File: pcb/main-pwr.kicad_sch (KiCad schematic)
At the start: 26 parts, among them U2 ADP5054

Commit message: power restructuring
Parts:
- removed C3, C4, C5, C6, C7: 0.1uF, Capacitor_SMD:C_0402_1005Metric, symbol library:C
- removed L1, L2, L3, L4: 1uH, Inductor_SMD:L_0402_1005Metric, symbol library:L
- removed R10, R8: 24K, Resistor_SMD:R_0402_1005Metric, symbol library:R_US
- removed R11, R14, R7: 30K, Resistor_SMD:R_0402_1005Metric, symbol library:R_US
- removed R12: 120K, Resistor_SMD:R_0402_1005Metric, symbol library:R_US
- removed R13: 15K, Resistor_SMD:R_0402_1005Metric, symbol library:R_US
- removed R15, R17: 100, Resistor_SMD:R_0402_1005Metric, symbol library:R_US
- removed R16: 0.005, Resistor_SMD:R_0603_1608Metric, symbol library:R_US
- removed R6: 31.6K, Resistor_SMD:R_0402_1005Metric, symbol library:R_US
- removed R9: 75K, Resistor_SMD:R_0402_1005Metric, symbol library:R_US
- removed U2: ADP5054, Package_DFN_QFN:QFN-48-1EP_7x7mm_P0.5mm_EP5.15x5.15mm, symbol library:ADP5054
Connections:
- net 5V0_SENS_N: now also C2.1, R3.1; no longer C2.2, R5.1
- net 5V0_SENS_P: now also C2.2, R5.1; no longer C2.1, R3.1
- no-connect marks 2 -> 0
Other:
- removed sheet Comp & Decpl.
- removed sheet Sequencing
- added sheet 1V0 (1v0.kicad_sch)
- added sheet 1V2 (1v2.kicad_sch)
- added sheet 1V35 (1v35.kicad_sch)
- added sheet 1V8 (1v8.kicad_sch)
- added sheet 3V3 (3v3.kicad_sch)
- note added: "Power sequencing: 1. 1V0_FD, 1V0_MGT 2. 1V8_FD 3. 1V2_MGT 4. 1V35_DDR, 3V3_FD"
- note removed: "Power sequencing: 1. 1V0_FD, 1V0_MGT 2. 1V8_FD 3. 1V2_MGT 4. 3V3_FD"
- note removed: "V_en = 0.811V"
- note removed: "vout = vref * (1 + rtop/rbot)"
- moved on the sheet: C2, R3, R4, R5

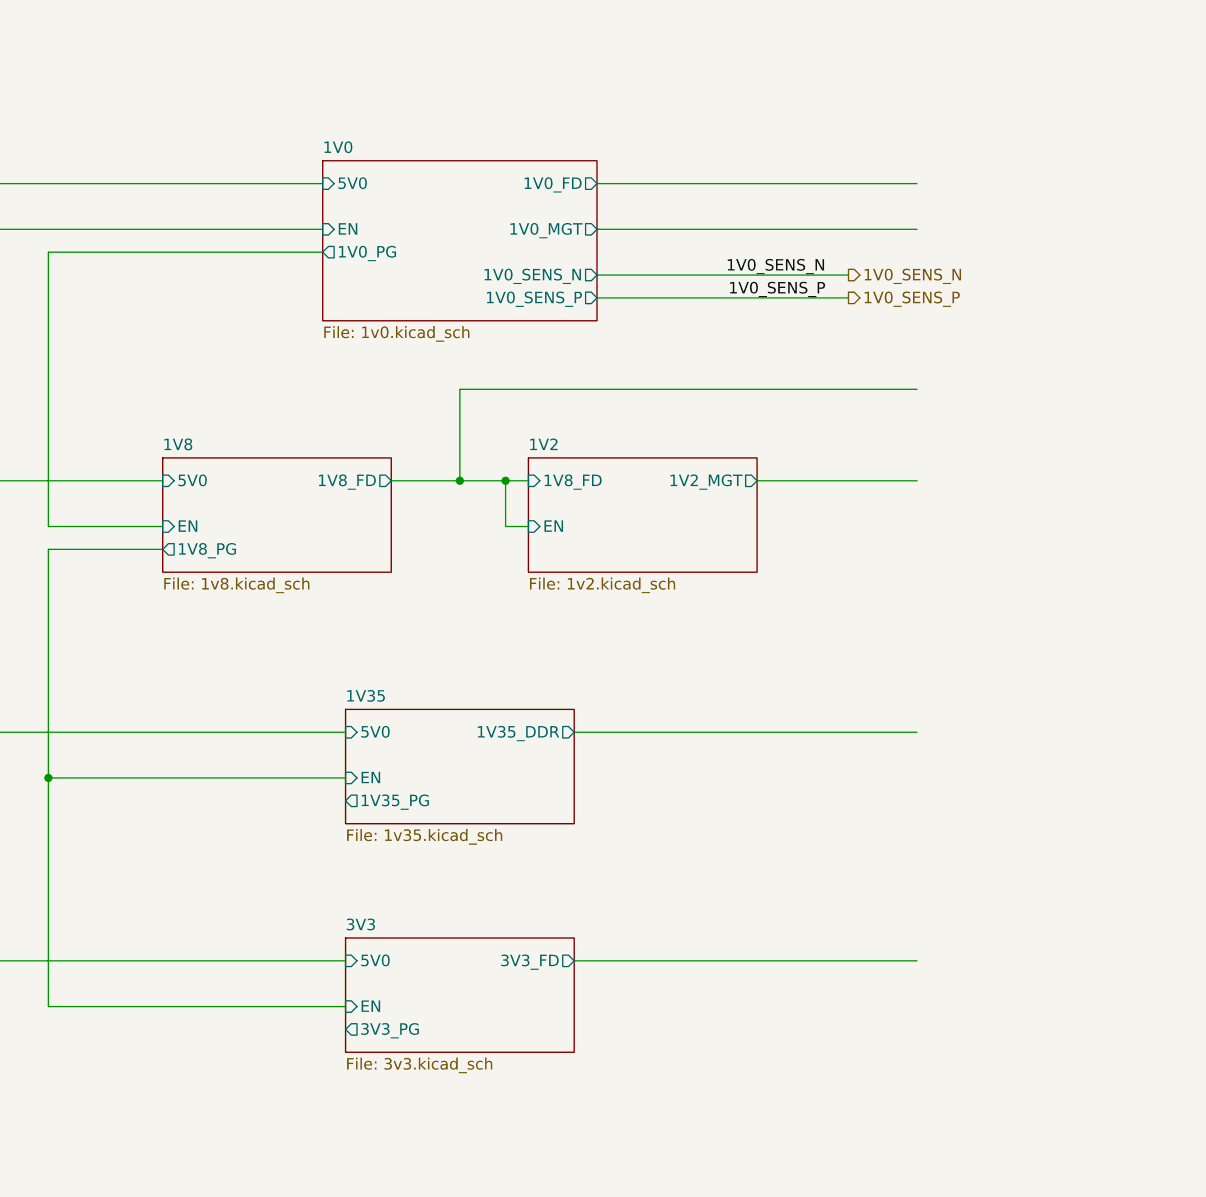
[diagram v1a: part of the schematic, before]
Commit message: changes to power tree
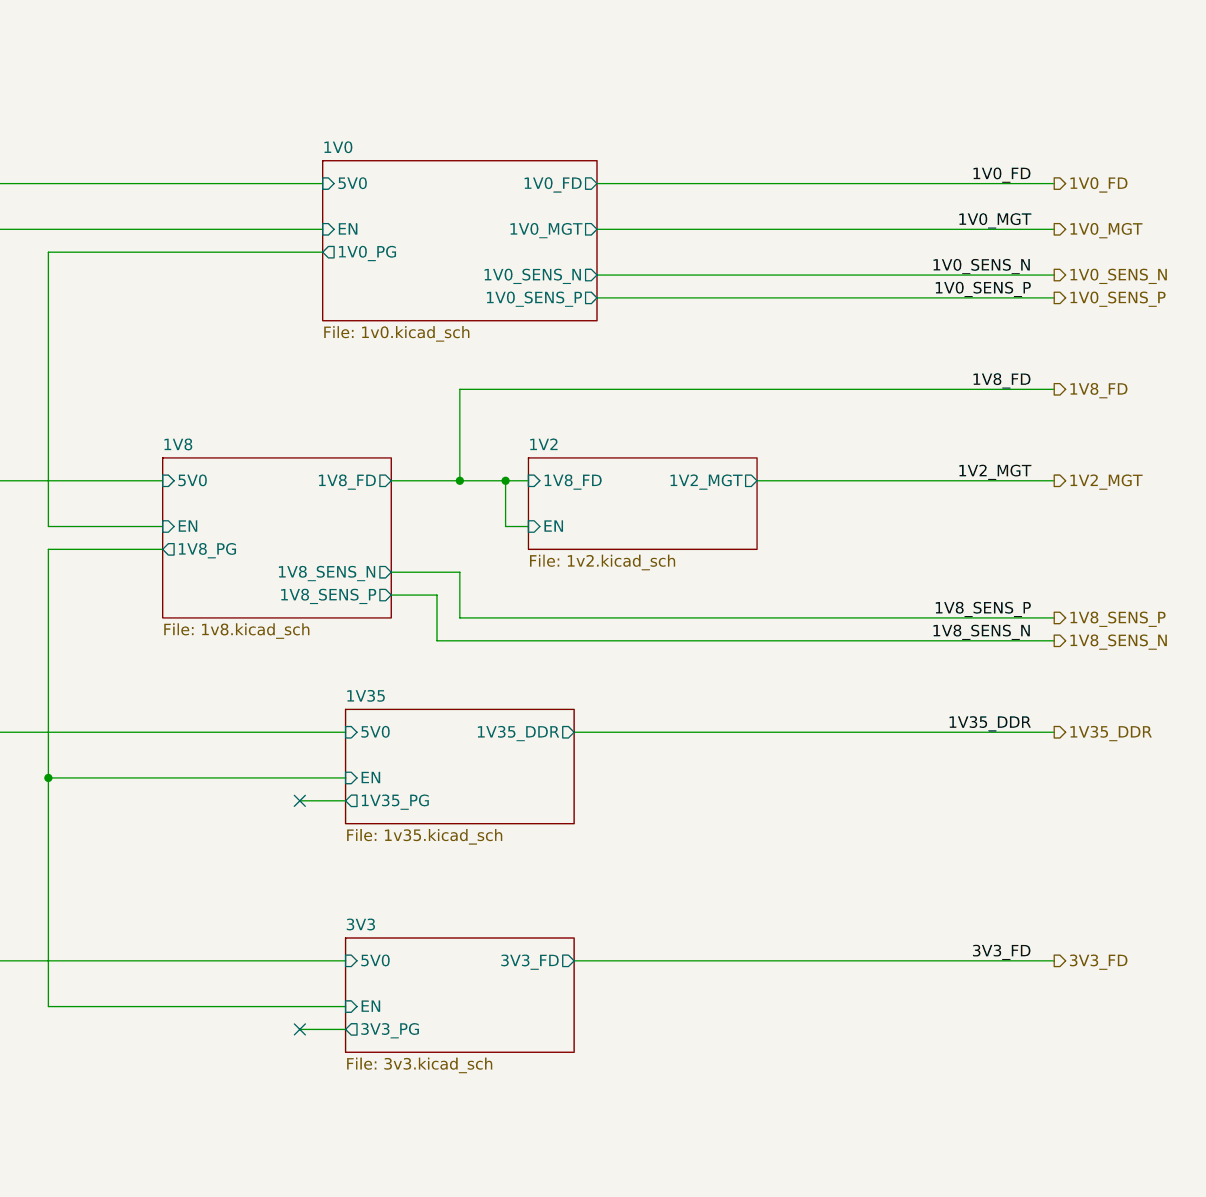
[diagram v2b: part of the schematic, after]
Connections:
- no-connect marks 0 -> 2
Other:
- sheet 1V8 ports: added 1V8_SENS_N, 1V8_SENS_P; removed none

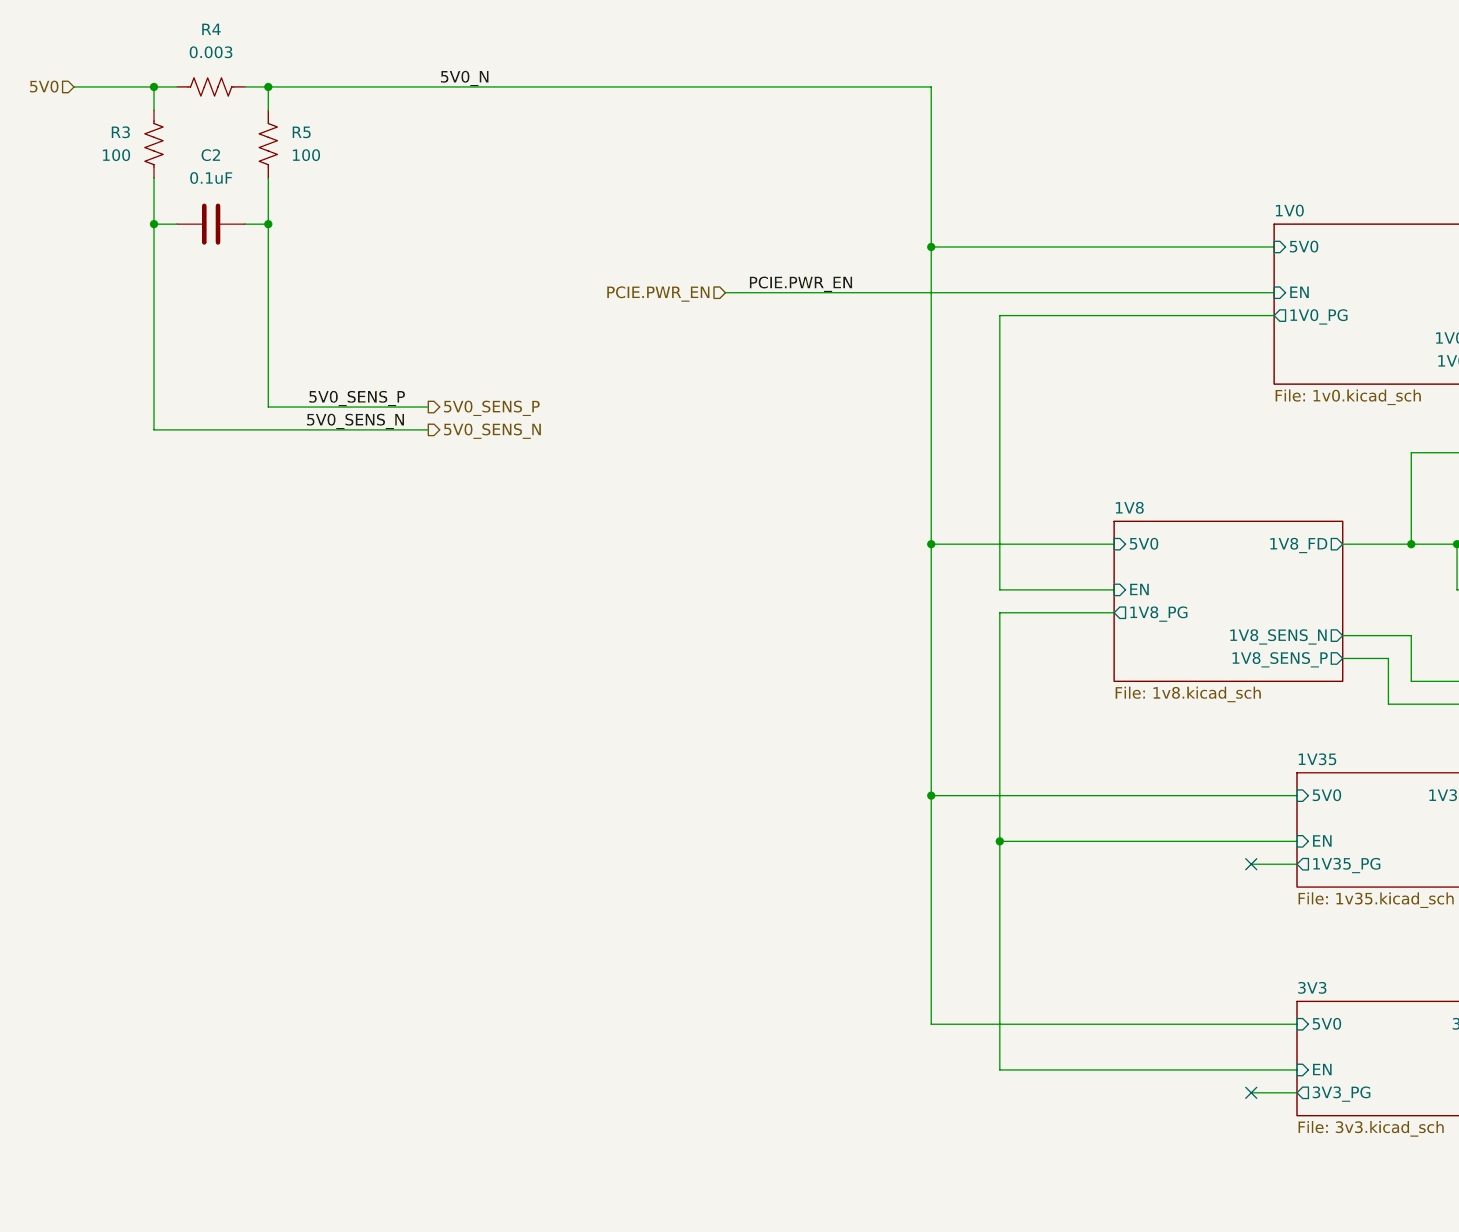
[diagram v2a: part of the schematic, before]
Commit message: moved stuff around, bom
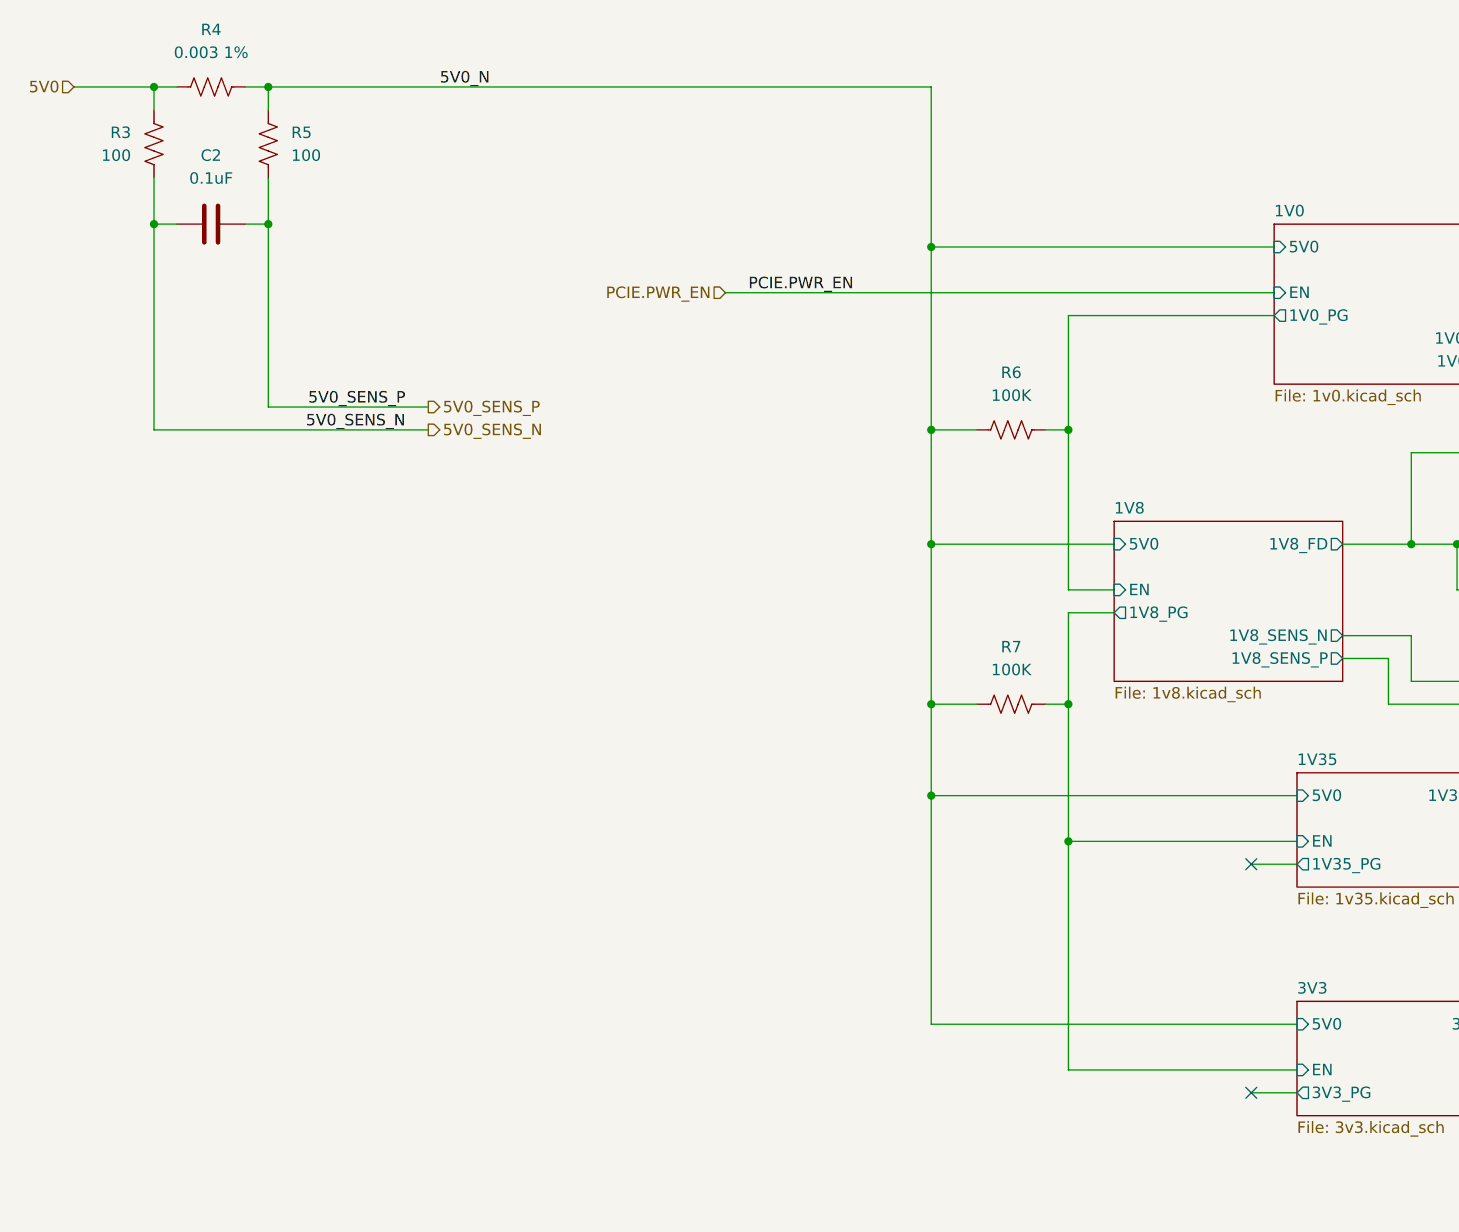
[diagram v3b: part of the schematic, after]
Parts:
- added R6, R7: 100K, library:R_0402_1005Metric, symbol library:R_US
- C2: Manufacturer (none) -> KEMET; Manufacturer Product Number (none) -> C0402C104K4RACTU
- R3, R5: Manufacturer (none) -> YAGEO; Manufacturer Product Number (none) -> RC0402FR-07100RL
- R4: value 0.003 -> 0.003 1%; footprint Resistor_SMD:R_0805_2012Metric -> Resistor_SMD:R_1206_3216Metric; Manufacturer (none) -> Vishay Dale; Manufacturer Product Number (none) -> WSKW06123L000FEA
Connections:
- net 1V0/1V0_PG: now also R6.2
- net 1V35/EN: now also R7.2
- net 5V0_N: now also R6.1, R7.1

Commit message: jtag, dcplng
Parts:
- added R29: 100K, library:R_0402_1005Metric, symbol library:R_US
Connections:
- net 5V0_N: now also R29.1
- new net 3V3_PG: R29.2
- no-connect marks 2 -> 1
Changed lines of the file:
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@@
 	)
 	(junction
-		(at 119.38 104.14)
+		(at 121.92 104.14)
 		(diameter 0)
 		(color 255 0 0 1)
@@
 	)
 	(junction
-		(at 119.38 93.98)
+		(at 134.62 142.24)
+		(diameter 0)
+		(color 0 0 0 0)
+	)
+	(junction
+		(at 121.92 93.98)
 		(diameter 0)
 		(color 255 0 0 1)
@@
 	)
 	(junction
-		(at 119.38 63.5)
+		(at 121.92 63.5)
 		(diameter 0)
 		(color 255 0 0 1)
 	)
 	(junction
-		(at 119.38 76.2)
+		(at 121.92 76.2)
 		(diameter 0)
 		(color 255 0 0 1)
@@
 	)
 	(junction
-		(at 119.38 43.18)
+		(at 121.92 43.18)
 		(diameter 0)
 		(color 255 0 0 1)
@@
 	)
 	(junction
+		(at 121.92 129.54)
+		(diameter 0)
+		(color 255 0 0 1)
+	)
+	(junction
 		(at 134.62 109.22)
 		(diameter 0)
@@
 	)
 	(no_connect
-		(at 154.94 137.16)
-	)
-	(no_connect
 		(at 154.94 111.76)
 	)
@@
 	(wire
 		(pts
-			(xy 119.38 93.98) (xy 124.46 93.98)
+			(xy 121.92 93.98) (xy 124.46 93.98)
 		)
 		(stroke
@@
 	(wire
 		(pts
+			(xy 134.62 142.24) (xy 134.62 147.32)
+		)
+		(stroke
+			(width 0)
+			(type default)
+		)
+	)
+	(wire
+		(pts
 			(xy 187.96 48.26) (xy 238.76 48.26)
 		)
@@
 	(wire
 		(pts
-			(xy 154.94 137.16) (xy 160.02 137.16)
+			(xy 121.92 129.54) (xy 121.92 142.24)
+		)
+		(stroke
+			(width 0.3556)
+			(type default)
+			(color 255 0 0 1)
+		)
+	)
+	(wire
+		(pts
+			(xy 134.62 137.16) (xy 160.02 137.16)
 		)
 		(stroke
@@
 	(wire
 		(pts
+			(xy 132.08 142.24) (xy 134.62 142.24)
+		)
+		(stroke
+			(width 0)
+			(type default)
+		)
+	)
+	(wire
+		(pts
 			(xy 172.72 76.2) (xy 172.72 66.04)
 		)
@@
 	(wire
 		(pts
-			(xy 119.38 93.98) (xy 119.38 104.14)
+			(xy 121.92 93.98) (xy 121.92 104.14)
 		)
 		(stroke
@@
 	(wire
 		(pts
+			(xy 121.92 142.24) (xy 124.46 142.24)
+		)
+		(stroke
+			(width 0.3556)
+			(type default)
+			(color 255 0 0 1)
+		)
+	)
+	(wire
+		(pts
 			(xy 177.8 76.2) (xy 180.34 76.2)
 		)
@@
 	(wire
 		(pts
-			(xy 119.38 76.2) (xy 119.38 93.98)
+			(xy 134.62 147.32) (xy 238.76 147.32)
+		)
+		(stroke
+			(width 0)
+			(type default)
+		)
+	)
+	(wire
+		(pts
+			(xy 121.92 76.2) (xy 121.92 93.98)
 		)
 		(stroke
@@
 	(wire
 		(pts
-			(xy 45.72 25.4) (xy 119.38 25.4)
+			(xy 45.72 25.4) (xy 121.92 25.4)
 		)
 		(stroke
@@
 	(wire
 		(pts
-			(xy 119.38 25.4) (xy 119.38 43.18)
+			(xy 121.92 25.4) (xy 121.92 43.18)
 		)
 		(stroke
@@
 	(wire
 		(pts
-			(xy 119.38 43.18) (xy 119.38 63.5)
+			(xy 121.92 43.18) (xy 121.92 63.5)
 		)
 		(stroke
@@
 	(wire
 		(pts
-			(xy 119.38 63.5) (xy 124.46 63.5)
+			(xy 121.92 63.5) (xy 124.46 63.5)
 		)
 		(stroke
@@
 	(wire
 		(pts
-			(xy 119.38 76.2) (xy 139.7 76.2)
+			(xy 121.92 76.2) (xy 139.7 76.2)
 		)
 		(stroke
@@
 	(wire
 		(pts
+			(xy 134.62 137.16) (xy 134.62 142.24)
+		)
+		(stroke
+			(width 0)
+			(type default)
+		)
+	)
+	(wire
+		(pts
 			(xy 154.94 111.76) (xy 160.02 111.76)
 		)
@@
 	(wire
 		(pts
-			(xy 119.38 43.18) (xy 157.48 43.18)
+			(xy 121.92 43.18) (xy 157.48 43.18)
 		)
 		(stroke
@@
 	(wire
 		(pts
-			(xy 119.38 63.5) (xy 119.38 76.2)
+			(xy 121.92 63.5) (xy 121.92 76.2)
 		)
 		(stroke
@@
 	(wire
 		(pts
-			(xy 119.38 104.14) (xy 119.38 129.54)
+			(xy 121.92 104.14) (xy 121.92 129.54)
 		)
 		(stroke
@@
 	(wire
 		(pts
-			(xy 119.38 104.14) (xy 160.02 104.14)
+			(xy 121.92 104.14) (xy 160.02 104.14)
 		)
 		(stroke
@@
 	(wire
 		(pts
-			(xy 119.38 129.54) (xy 160.02 129.54)
+			(xy 121.92 129.54) (xy 160.02 129.54)
 		)
 		(stroke
@@
 		(shape output)
 		(at 238.76 76.2 0)
+		(effects
+			(font
+				(size 1.27 1.27)
+			)
+			(justify left)
+		)
+	)
+	(hierarchical_label "3V3_PG"
+		(shape output)
+		(at 238.76 147.32 0)
 		(effects
 			(font
@@
 	(symbol
 		(lib_id "library:R_US")
+		(at 128.27 142.24 90)
+		(unit 1)
+		(exclude_from_sim no)
+		(in_bom yes)
+		(on_board yes)
+		(dnp no)
+		(fields_autoplaced yes)
+		(property "Reference" "R29"
+			(at 128.27 135.89 90)
+			(effects
+				(font
+					(size 1.27 1.27)
+				)
+			)
+		)
+		(property "Value" "100K"
+			(at 128.27 138.43 90)
+			(effects
+				(font
+					(size 1.27 1.27)
+				)
+			)
+		)
+		(property "Footprint" "library:R_0402_1005Metric"
+			(at 128.524 141.224 90)
+			(effects
+				(font
+					(size 1.27 1.27)
+				)
+				(hide yes)
+			)
+		)
+		(property "Datasheet" "~"
+			(at 128.27 142.24 0)
+			(effects
+				(font
+					(size 1.27 1.27)
+				)
+				(hide yes)
+			)
+		)
+		(property "Description" "RES 100K OHM 1% 1/16W 0402"
+			(at 128.27 142.24 0)
+			(effects
+				(font
+					(size 1.27 1.27)
+				)
+				(hide yes)
+			)
+		)
+		(property "Manufacturer" "YAGEO"
+			(at 128.27 142.24 0)
+			(effects
+				(font
+					(size 1.27 1.27)
+				)
+				(hide yes)
+			)
+		)
+		(property "Manufacturer Product Number" "RC0402FR-07100KL"
+			(at 128.27 142.24 90)
+			(effects
+				(font
+					(size 1.27 1.27)
+				)
+				(hide yes)
+			)
+		)
+		(pin "2"
+		)
+		(pin "1"
+		)
+		(instances
+			(project "RPi-HwAB-1"
+				(path "/e63e39d7-6ac0-4ffd-8aa3-1841a4541b55/f9ebb56c-78c7-42ac-bc19-ccbf788f5318"
+					(reference "R29")
+					(unit 1)
+				)
+			)
+		)
+	)
+	(symbol
+		(lib_id "library:R_US")
 		(at 39.37 25.4 90)
 		(unit 1)
@@
 		)
 		(fill
-			(color 0 0 0 0.0000)
+			(color 132 0 0 0.0588)
 		)
 		(property "Sheetname" "1V2"
@@
 		)
 		(fill
-			(color 0 0 0 0.0000)
+			(color 132 0 0 0.0588)
 		)
 		(property "Sheetname" "1V8"
@@
 		)
 		(fill
-			(color 0 0 0 0.0000)
+			(color 132 0 0 0.0600)
 		)
 		(property "Sheetname" "1V0"
@@
 		)
 		(fill
-			(color 0 0 0 0.0000)
+			(color 132 0 0 0.0588)
 		)
 		(property "Sheetname" "3V3"
@@
 		)
 		(fill
-			(color 0 0 0 0.0000)
+			(color 132 0 0 0.0588)
 		)
 		(property "Sheetname" "1V35"

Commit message: decoupling
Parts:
- R3, R5: value 100 -> 10; Manufacturer Product Number RC0402FR-07100RL -> RC0402FR-0710RL
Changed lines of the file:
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@@
 			)
 		)
-		(property "Value" "100"
+		(property "Value" "10"
 			(at 48.26 33.02 0)
 			(effects
@@
 			)
 		)
-		(property "Description" "RES 100 OHM 1% 1/16W 0402"
+		(property "Description" "RES 10 OHM 1% 1/16W 0402"
 			(at 45.72 31.75 0)
 			(effects
@@
 			)
 		)
-		(property "Manufacturer Product Number" "RC0402FR-07100RL"
+		(property "Manufacturer Product Number" "RC0402FR-0710RL"
+			(at 45.72 31.75 0)
+			(effects
+				(font
+					(size 1.27 1.27)
+				)
+				(hide yes)
+			)
+		)
+		(property "Name" ""
 			(at 45.72 31.75 0)
 			(effects
@@
 			)
 		)
-		(property "Value" "100"
+		(property "Value" "10"
 			(at 30.48 33.02 0)
 			(effects
@@
 			)
 		)
-		(property "Description" "RES 100 OHM 1% 1/16W 0402"
+		(property "Description" "RES 10 OHM 1% 1/16W 0402"
 			(at 33.02 31.75 0)
 			(effects
@@
 			)
 		)
-		(property "Manufacturer Product Number" "RC0402FR-07100RL"
+		(property "Manufacturer Product Number" "RC0402FR-0710RL"
 			(at 33.02 31.75 0)
 			(effects
+				(font
+					(size 1.27 1.27)
+				)
+				(hide yes)
+			)
+		)
+		(property "Name" ""
+			(at 33.02 31.75 0)
+			(effects
